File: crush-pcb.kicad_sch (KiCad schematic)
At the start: 12 parts, among them J1 USB_B_Micro, J2 3x3 Header, J3 3x3 Header, J4 3x3 Header, J5 3x2 Header, U1 Teensy4.1, U2 ISO7740DW, U3 ISO7740DW

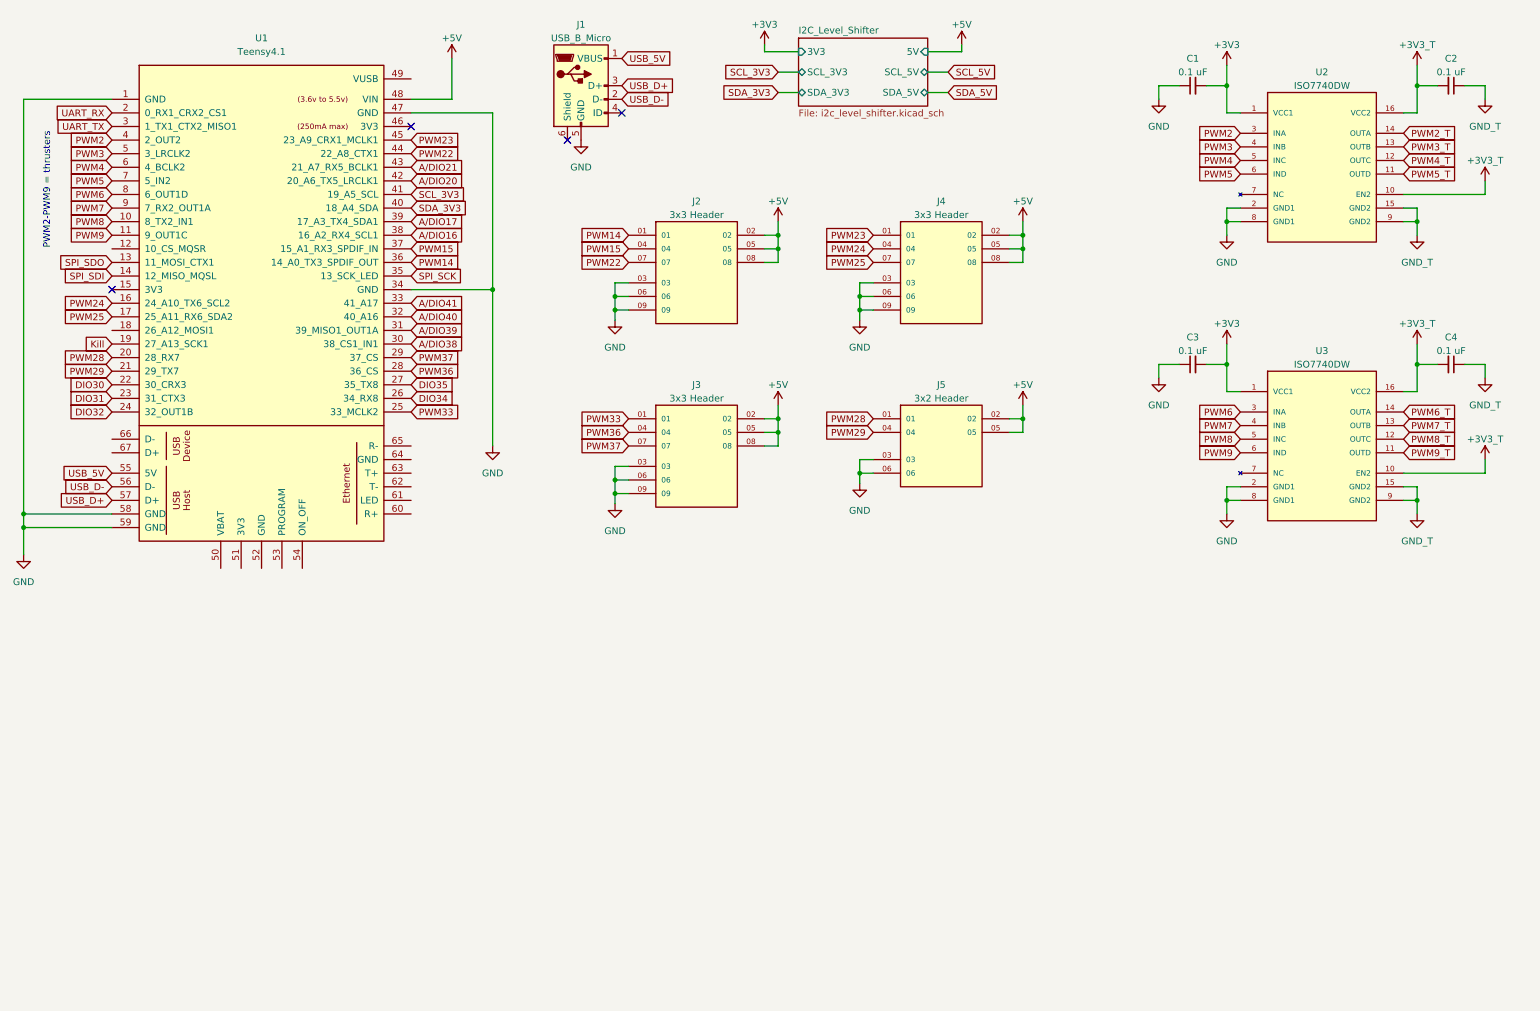
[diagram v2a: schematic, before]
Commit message: Header Arrangement
Add headers for the remaining pins and attach the custom footprints
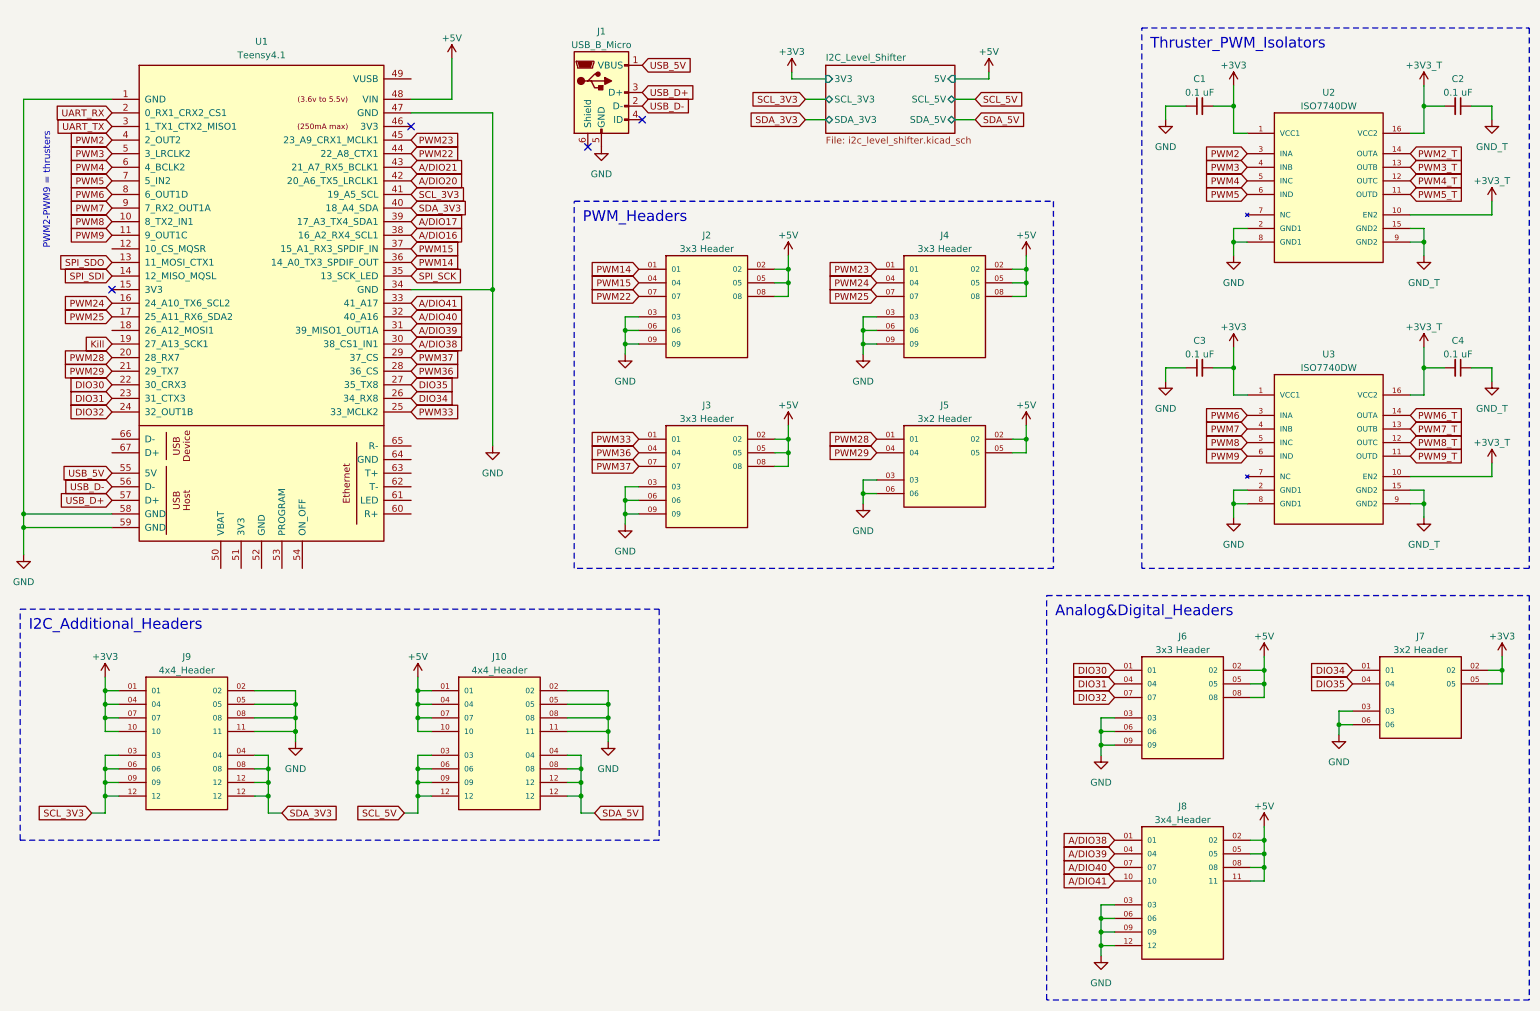
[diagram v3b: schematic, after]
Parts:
- added J10, J9: 4x4_Header, Crush_Mainboard_Footprints:4x4_Header, symbol Crush_MainBoard_Symbols:4x4_Header
- added J6: 3x3 Header, symbol Crush_MainBoard_Symbols:3x3_Header
- added J7: 3x2 Header, Crush_Mainboard_Footprints:3x2 header, symbol CrushMainBoard_Library:3x2_Header
- added J8: 3x4_Header, symbol Crush_MainBoard_Symbols:3x4_Header
- J2, J3, J4: footprint (none) -> Crush_Mainboard_Footprints:3x3 header
- J5: footprint (none) -> Crush_Mainboard_Footprints:3x2 header
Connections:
- net +3V3: now also J7.02, J7.05
- net +5V: now also J10.01, J10.04, J10.07, J10.10, J6.02, J6.05, J6.08, J8.02, J8.05, J8.08, J8.11, J9.01, J9.04, J9.07, J9.10
- net A/DIO38: now also J8.01
- net A/DIO39: now also J8.04
- net A/DIO40: now also J8.07
- net A/DIO41: now also J8.10
- net DIO30: now also J6.01
- net DIO31: now also J6.04
- net DIO32: now also J6.07
- net DIO34: now also J7.01
- net DIO35: now also J7.04
- net GND: now also J10.02, J10.05, J10.08, J10.11, J6.03, J6.06, J6.09, J7.03, J7.06, J8.03, J8.06, J8.09, J8.12, J9.02, J9.05, J9.08, J9.11
- net SCL_3V3: now also J9.03, J9.06, J9.09, J9.12
- net SCL_5V: now also J10.03, J10.06, J10.09, J10.12
- net SDA_3V3: now also J9.04, J9.08, J9.12
- net SDA_5V: now also J10.04, J10.08, J10.12
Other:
- moved on the sheet: C1, C2, C3, C4, J1, J2, J3, J4, J5, U2, U3
